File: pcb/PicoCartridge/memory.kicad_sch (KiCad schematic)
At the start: 1 part, among them J3 Micro_SD_Card

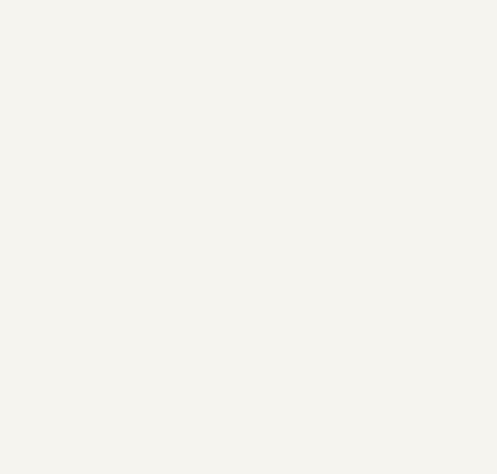
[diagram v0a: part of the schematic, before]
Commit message: Defined additional interfaces
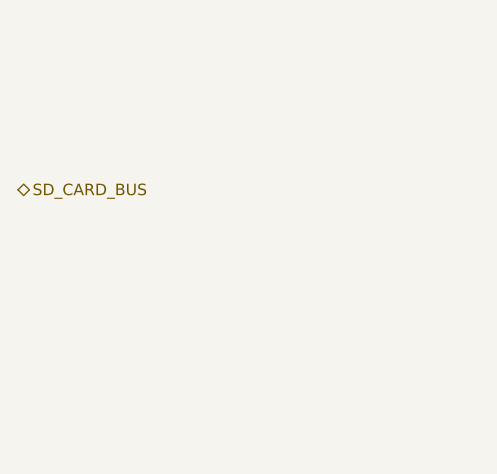
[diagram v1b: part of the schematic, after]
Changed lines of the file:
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@@
+		)
+	)
+	(hierarchical_label "SD_CARD_BUS"
+		(shape bidirectional)
+		(at 78.74 82.55 0)
+		(fields_autoplaced yes)
+		(effects
+			(font
+				(size 1.27 1.27)
+			)
+			(justify left)
 		)
 	)

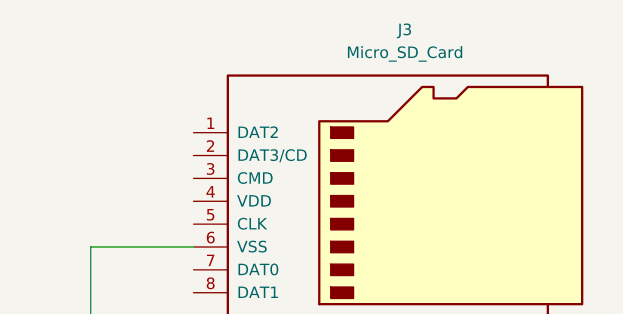
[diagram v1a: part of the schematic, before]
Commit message: Added base pcb layout
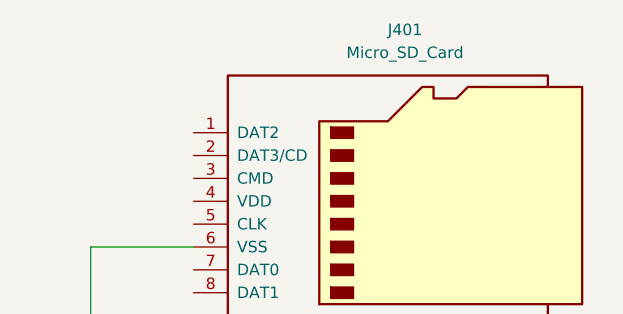
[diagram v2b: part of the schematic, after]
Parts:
- renumbered J3 to J401
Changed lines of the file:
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@@
 		(dnp no)
 		(fields_autoplaced yes)
-		(property "Reference" "J3"
+		(property "Reference" "J401"
 			(at 173.355 64.77 0)
 			(effects
@@
 			(project ""
 				(path "/369b8492-ac84-4ba1-9646-4010d0ed9f44/864b71b1-fdd0-4b9b-bab0-5640e9a99f9f"
-					(reference "J3")
+					(reference "J401")
 					(unit 1)
 				)

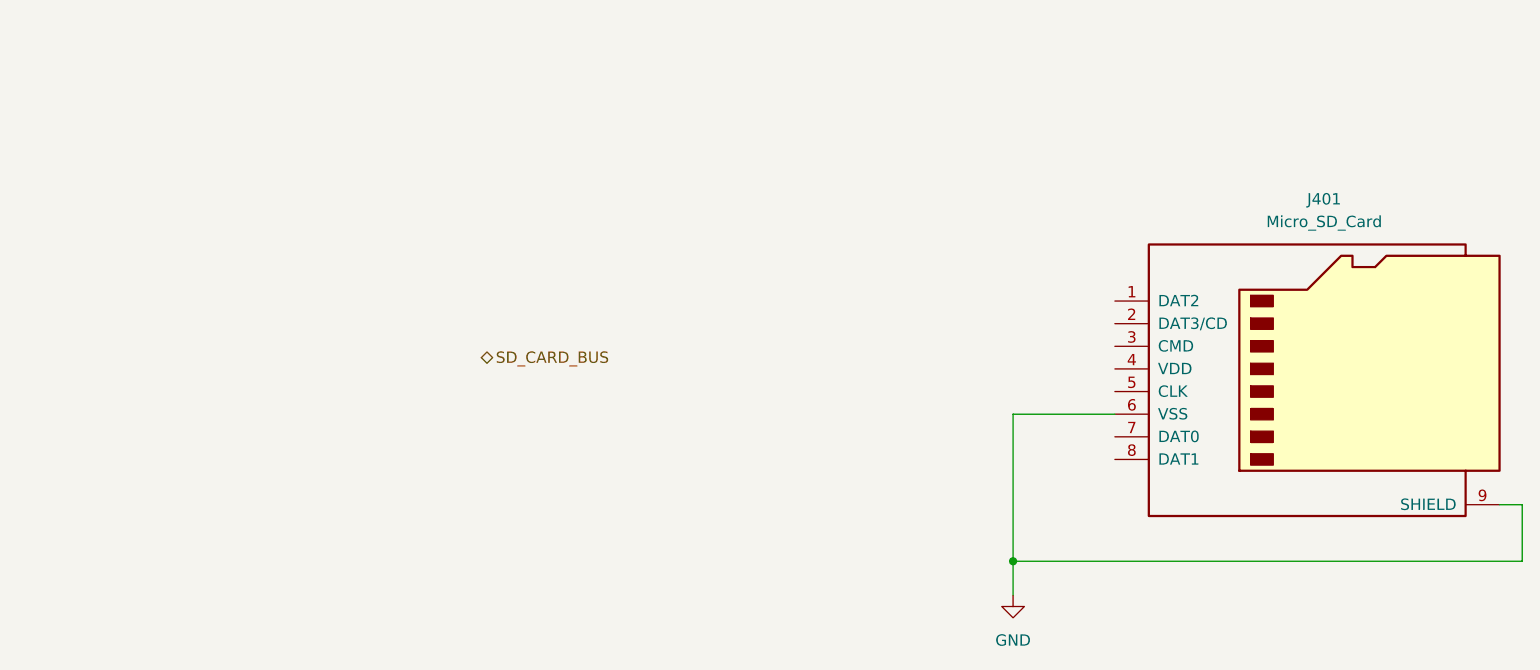
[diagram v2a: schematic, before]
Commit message: Added nets from main sheet
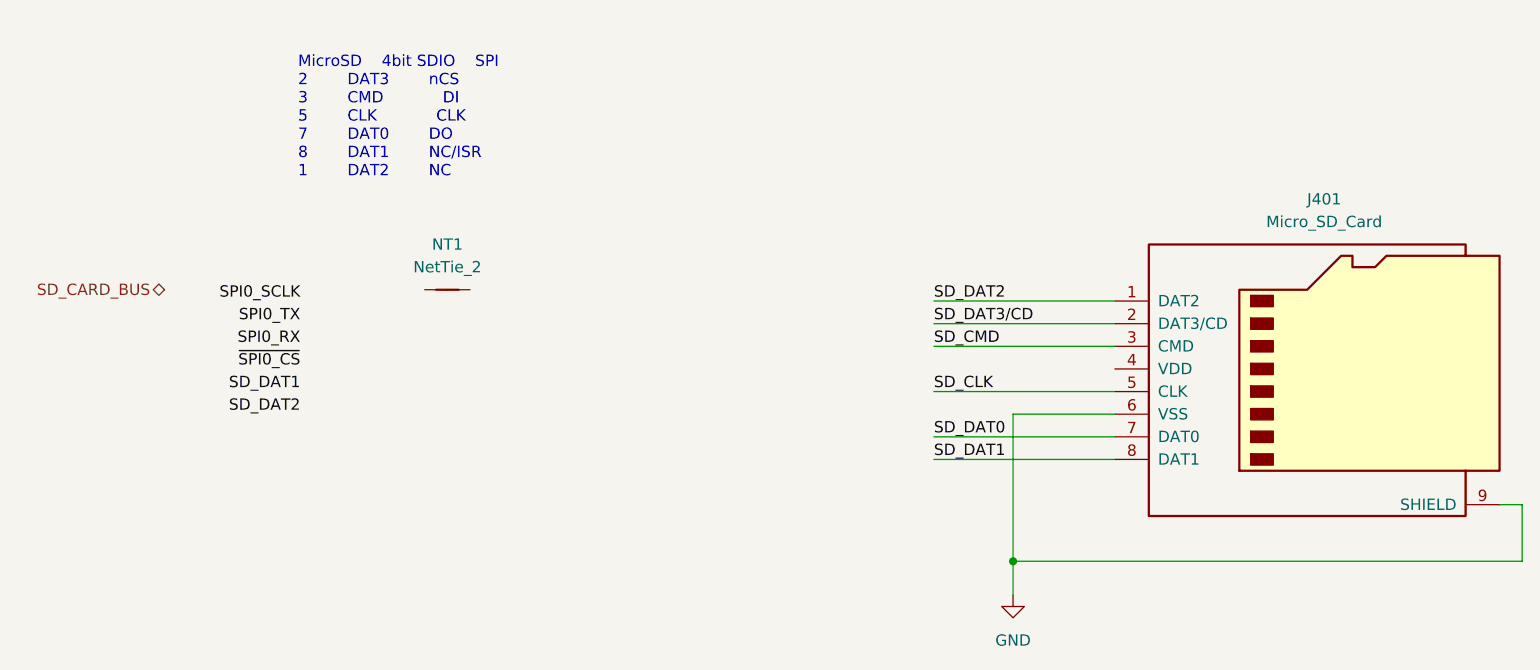
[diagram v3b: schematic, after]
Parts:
- added NT1: NetTie_2, symbol Device:NetTie_2
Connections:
- net SD_DAT2: now reaches J401.1 (DAT2)
- net SD_DAT3/CD: now reaches J401.2 (DAT3/CD)
- net SD_CMD: now reaches J401.3 (CMD)
- net SD_CLK: now reaches J401.5 (CLK)
- net SD_DAT0: now reaches J401.7 (DAT0)
- net SD_DAT1: now reaches J401.8 (DAT1)
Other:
- note added: "MicroSD 4bit SDIO SPI 2 DAT3 nCS 3 CMD DI 5 CLK CLK 7 DAT0 DO 8 DAT1 NC/ISR 1 DAT2 NC"

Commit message: Fixed connection between MCU and SD card
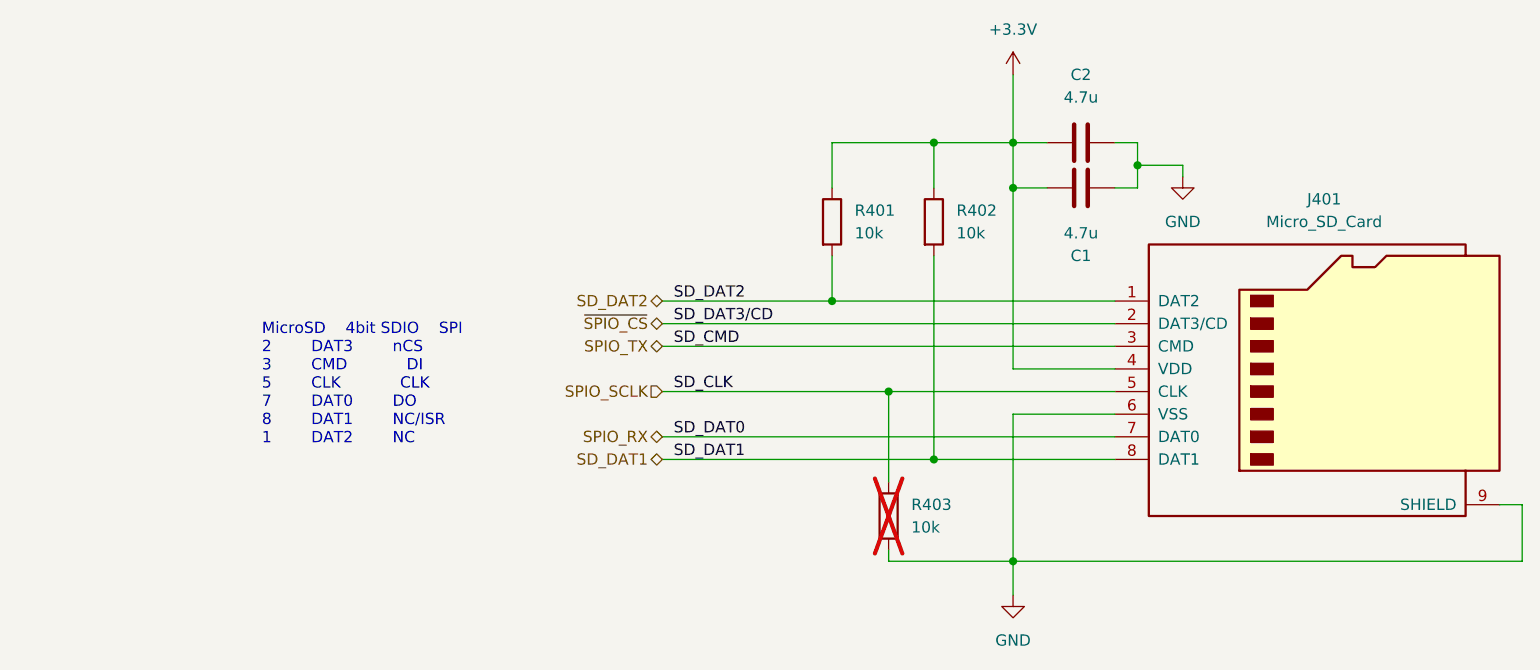
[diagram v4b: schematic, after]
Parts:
- removed NT1: NetTie_2, symbol Device:NetTie_2
- added C1, C2: 4.7u, Capacitor_SMD:C_0402_1005Metric, symbol Device:C
- added R401, R402, R403: 10k, Resistor_SMD:R_0402_1005Metric, symbol Device:R
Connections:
- net GND: now also C1.2, C2.1, R403.2
- net SD_DAT1: now also R402.2
- net SD_DAT2: now also R401.2
- net +3.3V: now reaches J401.4 (VDD)
- net +3.3V: now also C1.1, C2.2, R401.1, R402.1
- net SD_CLK renamed SPIO_SCLK
- net SPIO_SCLK: now also R403.1
- net SD_CMD renamed SPIO_TX
- net SD_DAT0 renamed SPIO_RX
- net SD_DAT3/CD renamed ~{SPIO_CS}
